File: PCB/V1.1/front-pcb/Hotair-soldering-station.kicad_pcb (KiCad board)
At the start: 2 copper layers, 70 x 120 mm, 60 parts, among them J2 main-board-conn, J3 hot_on, J4 solder_on, Q1 BC817, Q10 BC807, Q11 BC807, Q12 BC807, Q13 BC807, Q14 BC807, Q2 BC817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

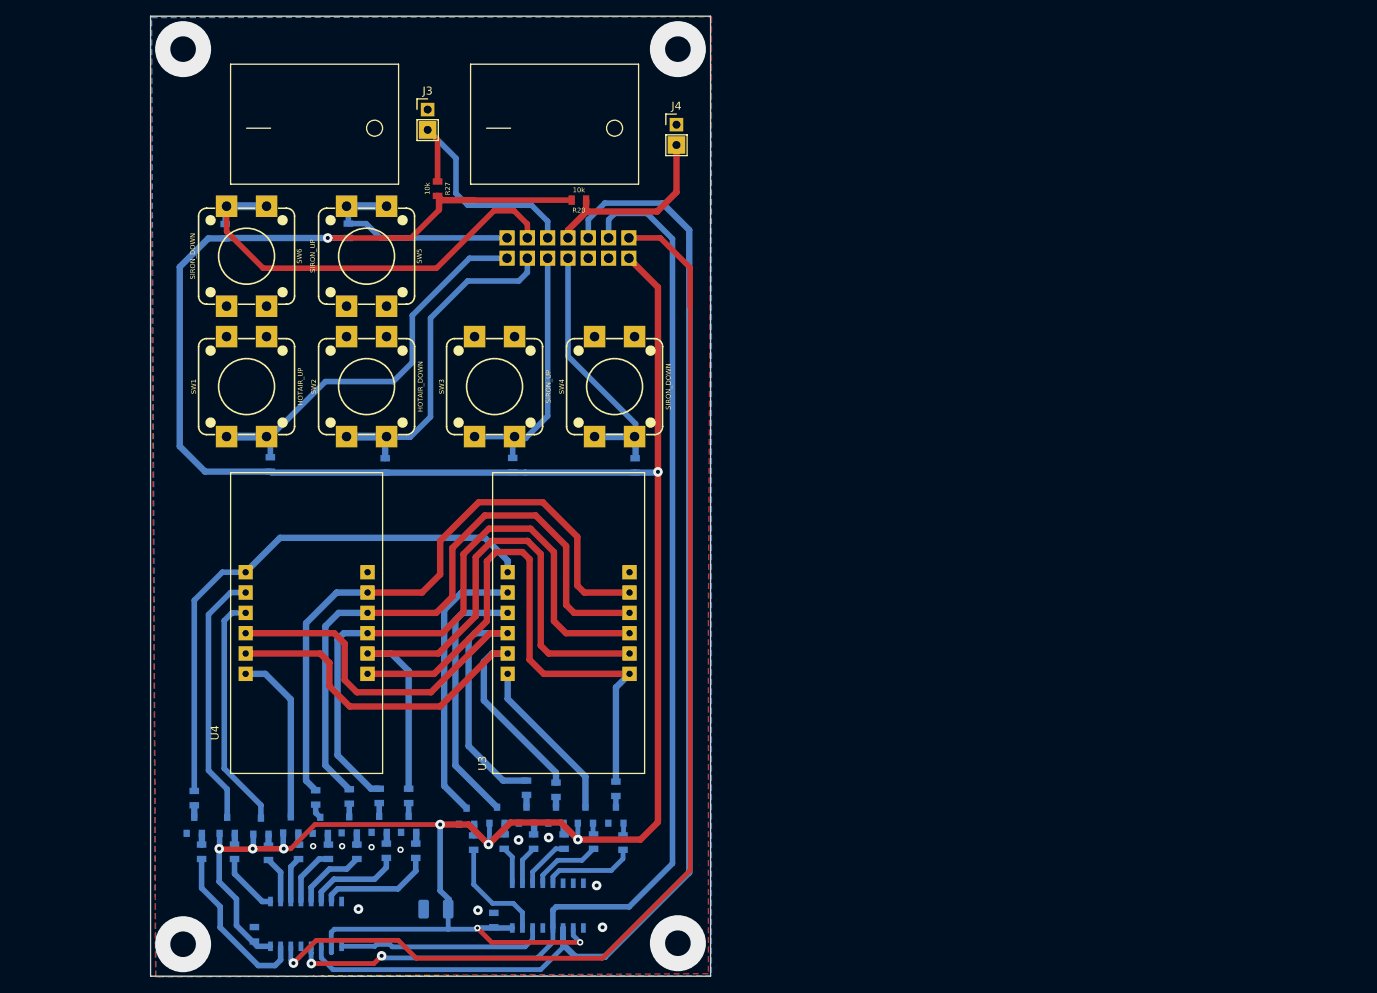
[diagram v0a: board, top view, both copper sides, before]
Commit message: Display change to LCD
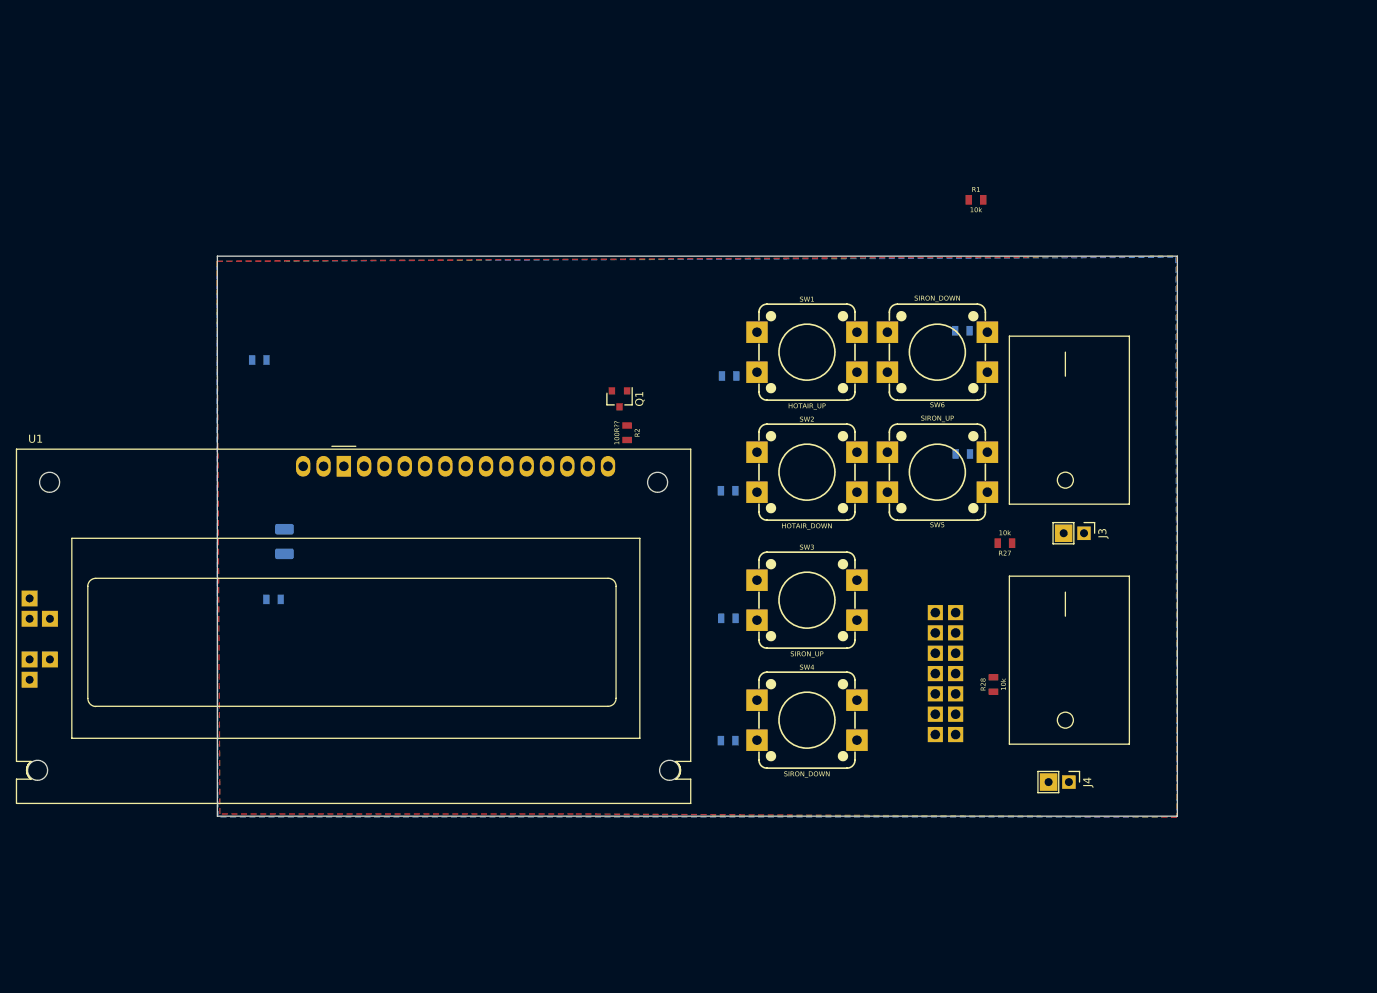
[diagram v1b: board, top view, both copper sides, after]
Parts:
- removed Q10, Q11, Q12, Q13, Q14, Q9: BC807, Package_TO_SOT_SMD:SOT-23
- removed Q2, Q3, Q4, Q5, Q6, Q7, Q8: BC817, Package_TO_SOT_SMD:SOT-23
- removed R10, R11, R12, R13, R14, R15, R16, R9: 120R, Capacitors:0805
- removed R17, R18, R19, R20, R21, R22, R3, R4, R5, R7, R8: 10k, Capacitors:0805
- removed R6: 5k6, Capacitors:0805
- removed U2: 74HC595D, Silicon-Standard:SO16
- removed U3: My-Footprints:3-digit-7-segment-display, My-Footprints:3-digit-7-segment-display
- removed U4: 3-dig-7-seg-display-common-anode, My-Footprints:3-digit-7-segment-display
- Q1, R1: moved to F.Cu
- R2: value 10k -> 100R??; moved to F.Cu
- U1: value 74HC595D -> RC1602A; footprint Silicon-Standard:SO16 -> Display:RC1602A; moved to F.Cu
- moved R1 109.8 mm to (126.4, 39.8), turned to 0 degrees
- moved J3 97.7 mm to (139.9, 81.4), turned to 270 degrees
- moved J4 95.7 mm to (138.1, 112.5), turned to 270 degrees
- moved R30 93.0 mm to (124.7, 56.1), turned to 180 degrees
- moved SW6 87.2 mm to (121.6, 58.8), turned to 180 degrees
- moved R27 83.6 mm to (130.1, 82.7), turned to 180 degrees
- moved R29 81.7 mm to (124.8, 71.5), turned to 180 degrees
- moved R28 79.7 mm to (128.6, 100.4), turned to 90 degrees
- moved SW5 76.3 mm to (121.6, 73.8), turned to 180 degrees
- moved C2 71.8 mm to (36.9, 59.8), turned to 0 degrees
- moved SW1 70.2 mm to (105.3, 58.8), turned to 0 degrees
- moved J2 68.8 mm to (119.5, 108.4), turned to 0 degrees
- moved R2 64.3 mm to (82.8, 68.9), turned to 270 degrees
- moved Q1 61.1 mm to (81.9, 64.6), turned to 270 degrees
- moved R23 58.4 mm to (95.6, 61.8), turned to 180 degrees
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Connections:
- J2 pad 12: 7SEG_CLK -> (no net)
- J2 pad 13: 7SEG_LATCH -> (no net)
- J2 pad 14: 7SEG_DIN -> (no net)
- J2 pad 2: GND -> +5V
- R1 pad 1: SEG_DP -> (no net)
- R2 pad 1: SEG_G -> Net-(Q1-Pad3)
- R2 pad 2: Net-(Q2-Pad1) -> Net-(R2-Pad2)
- U1 pad 1: HOTAIR_DIG3 -> GND
- U1 pad 10: +3V3 -> (no net)
- U1 pad 11: 7SEG_CLK -> (no net)
- U1 pad 12: 7SEG_LATCH -> (no net)
- U1 pad 13: GND -> (no net)
- U1 pad 14: 7SEG_DIN -> (no net)
- U1 pad 15: SEG_B -> +3V3
- U1 pad 16: +3V3 -> Net-(R2-Pad2)
- U1 pad 2: HOTAIR_DIG2 -> +5V
- U1 pad 3: HOTAIR_DIG1 -> (no net)
- U1 pad 4: SEG_G -> (no net)
- U1 pad 5: SEG_C -> (no net)
- U1 pad 6: SEG_DP -> (no net)
- U1 pad 7: SEG_D -> (no net)
- U1 pad 8: GND -> (no net)
- U1 pad 9: Net-(U1-Pad9) -> (no net)
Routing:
- net +3V3: track 357.2 -> 0.00 mm, vias 10 -> 0
- net 7SEG_CLK: track 156.2 -> 0.00 mm
- net 7SEG_LATCH: track 145.1 -> 0.00 mm, vias 2 -> 0
- net 7SEG_DIN: track 143.0 -> 0.00 mm, vias 1 -> 0
- net Net-(R10-Pad2): track 78.8 -> 0.00 mm
- net Net-(R9-Pad2): track 78.4 -> 0.00 mm
- net Net-(R14-Pad2): track 78.3 -> 0.00 mm
- net Net-(R13-Pad2): track 76.2 -> 0.00 mm
- net Net-(R12-Pad2): track 71.3 -> 0.00 mm
- net Net-(R11-Pad2): track 69.1 -> 0.00 mm
- net Net-(R15-Pad2): track 68.9 -> 0.00 mm
- net Net-(R16-Pad2): track 62.2 -> 0.00 mm
- net HOTAIR_FAN_DOWN_SW: track 56.1 -> 0.00 mm
- net HOTAIR_UP_SW: track 49.9 -> 0.00 mm
- net HOTAIR_DOWN_SW: track 42.8 -> 0.00 mm
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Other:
- board size 70 x 120 mm -> 120 x 70 mm

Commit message: Pin assign to new STM32F103, front panel design to new case
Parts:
- removed C1, C2: 100n, Capacitors:0805
- removed C3: 47u, Capacitor_Tantalum_SMD:CP_EIA-3528-21_Kemet-B
- removed Q1: BC817, Package_TO_SOT_SMD:SOT-23
- removed U1: RC1602A, Display:RC1602A
- added J1: solder_select, Connector_PinHeader_2.54mm:PinHeader_1x02_P2.54mm_Vertical, F.Cu at (92.7, 93.1)
- added R3: 10k, Capacitors:0805, F.Cu at (88.0, 79.8)
- added R4: 10k, Capacitors:0805, F.Cu at (83.9, 82.4)
- added SW7: SIRON_DOWN, Switches:TACTILE_SWITCH_PTH_12MM, F.Cu at (76.8, 103.5)
- added SW8: SIRON_UP, Switches:TACTILE_SWITCH_PTH_12MM, F.Cu at (42.5, 104.1)
- added SW9: SIRON_DOWN, Switches:TACTILE_SWITCH_PTH_12MM, F.Cu at (59.1, 104.1)
- R2: value 100R?? -> 10k
- moved R1 83.9 mm to (68.3, 100.2)
- moved R2 10.9 mm to (83.9, 79.8), turned to 0 degrees
- moved J2 4.81 mm to (119.5, 113.2)
- moved R28 4.81 mm to (128.6, 105.2)
- moved R24 4.81 mm to (95.5, 96.9)
- moved R26 4.81 mm to (95.5, 112.2)
- moved SW3 4.81 mm to (105.3, 94.6)
- moved SW4 4.81 mm to (105.3, 109.6)
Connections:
- J2 pad 10: HOTAIR_ON_SW -> HOTAIR_DOWN_SW
- J2 pad 11: SOLDER_ON_SW -> HOTAIR_UP_SW
- J2 pad 12: (no net) -> SOLDER_SELECT_SW
- J2 pad 13: (no net) -> HOTAIR_ON_SW
- J2 pad 14: (no net) -> SOLDER_ON_SW
- J2 pad 2: +5V -> GND
- J2 pad 3: GND -> MENU_DOWN_SW
- J2 pad 4: SOLDER_DOWN_SW -> MENU_OK_SW
- J2 pad 5: SOLDER_UP_SW -> MENU_UP_SW
- J2 pad 6: HOTAIR_DOWN_SW -> SOLDER_DOWN_SW
- J2 pad 7: HOTAIR_UP_SW -> SOLDER_UP_SW
- R1 pad 1: (no net) -> MENU_DOWN_SW
- R1 pad 2: Net-(Q1-Pad1) -> +3V3
- R2 pad 1: Net-(Q1-Pad3) -> MENU_OK_SW
- R2 pad 2: Net-(R2-Pad2) -> +3V3
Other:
- net class Default removed

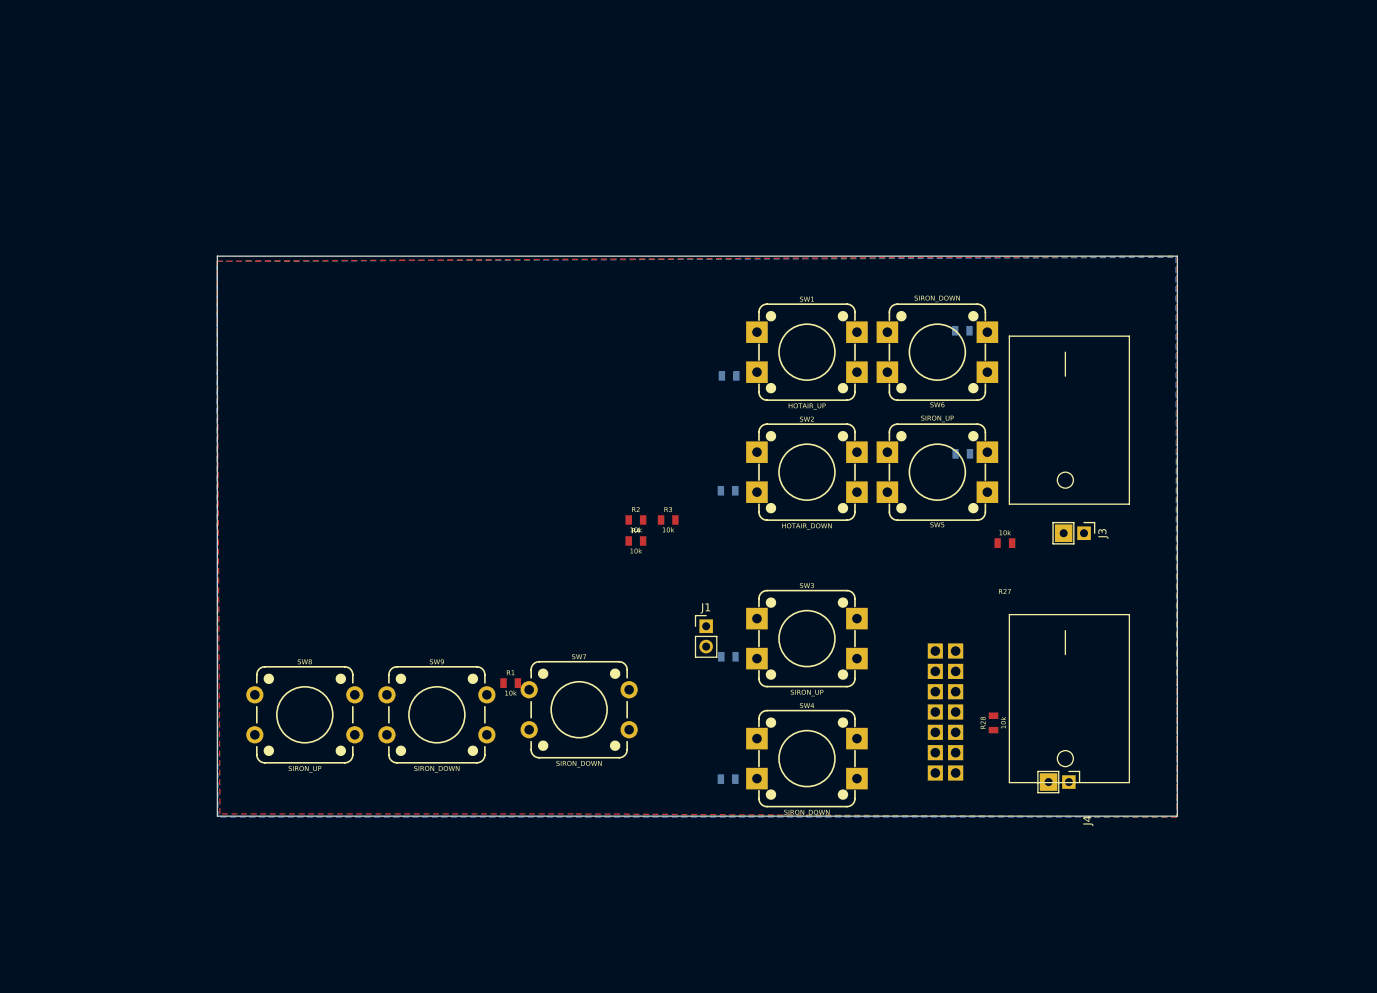
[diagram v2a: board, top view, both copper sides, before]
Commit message: Front Panel PCB design
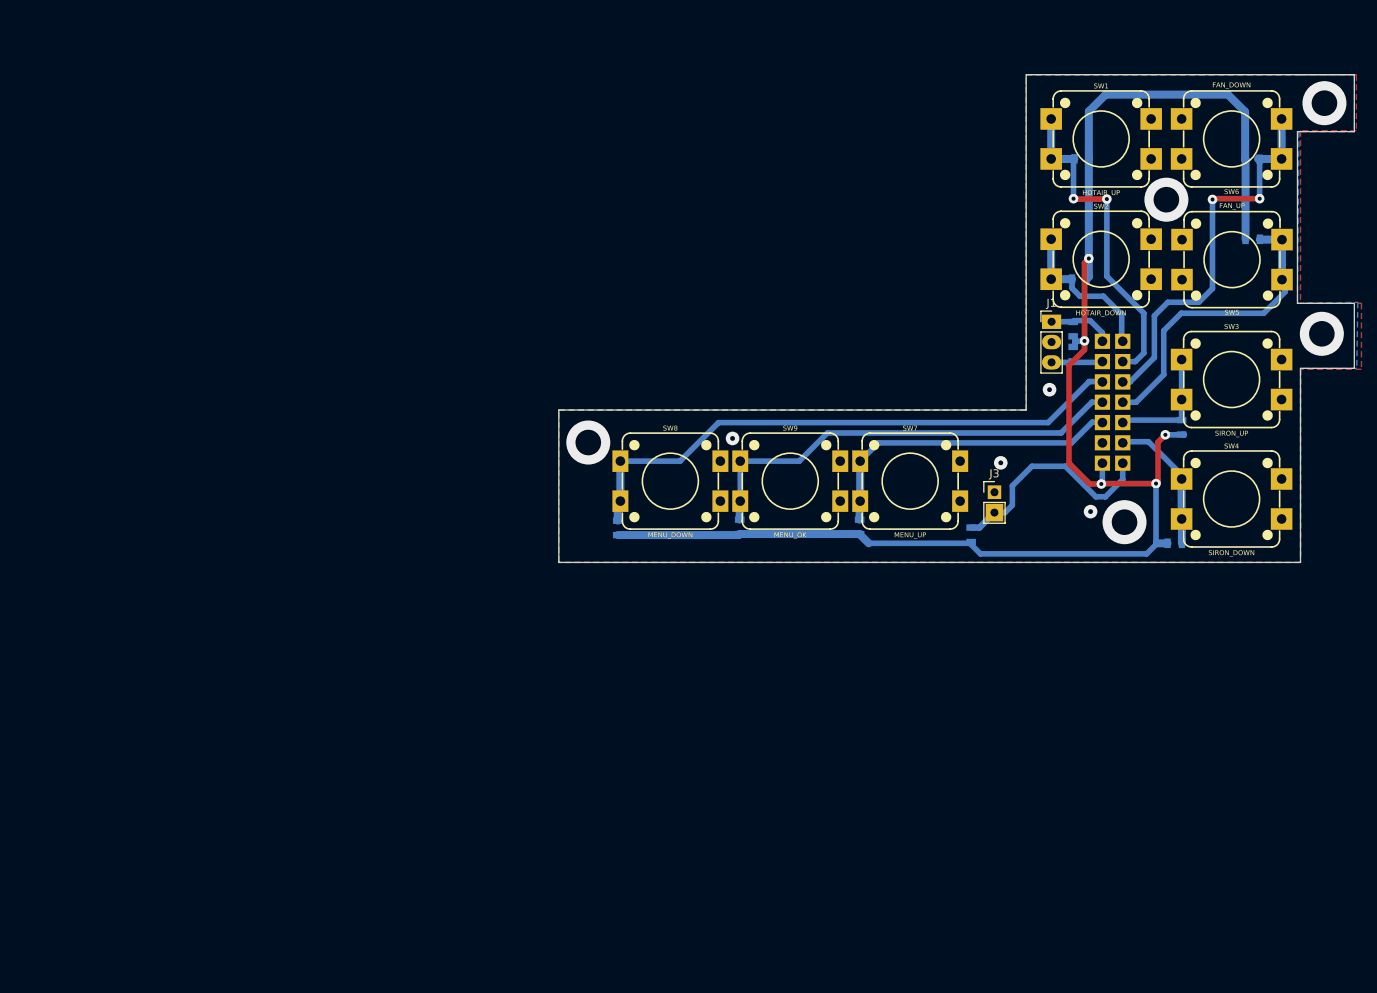
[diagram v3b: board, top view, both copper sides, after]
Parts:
- removed J4: solder_on, Connector_PinHeader_2.54mm:PinHeader_1x02_P2.54mm_Vertical
- J1: value solder_select -> Conn_01x03; footprint Connector_PinHeader_2.54mm:PinHeader_1x02_P2.54mm_Vertical -> Connector_PinHeader_2.54mm:PinHeader_1x03_P2.54mm_Vertical
- R1, R2, R27, R28, R3, R4: moved to B.Cu
- SW5: value SIRON_UP -> FAN_UP
- SW6: value SIRON_DOWN -> FAN_DOWN
- SW7: value SIRON_DOWN -> MENU_UP; footprint Switches:TACTILE_SWITCH_PTH_12MM -> My-Footprints:TACTILE_SWITCH_PTH_12MM
- SW8: value SIRON_UP -> MENU_DOWN; footprint Switches:TACTILE_SWITCH_PTH_12MM -> My-Footprints:TACTILE_SWITCH_PTH_12MM
- SW9: value SIRON_DOWN -> MENU_OK; footprint Switches:TACTILE_SWITCH_PTH_12MM -> My-Footprints:TACTILE_SWITCH_PTH_12MM
- moved R24 63.5 mm to (152.1, 68.2), turned to -90 degrees
- moved R26 63.1 mm to (151.3, 82.7)
- moved SW4 62.2 mm to (158.4, 77.2)
- moved SW3 62.2 mm to (158.4, 62.2)
- moved R4 60.7 mm to (138.6, 55.9), turned to -90 degrees
- moved J1 57.6 mm to (135.9, 55.0)
- moved SW8 54.2 mm to (88.2, 74.9)
- moved SW9 53.0 mm to (103.2, 74.9)
- moved R23 51.8 mm to (139.6, 34.6), turned to 0 degrees
- moved R25 51.2 mm to (139.3, 49.7), turned to 0 degrees
- moved SW7 50.3 mm to (118.2, 74.9)
- moved R28 47.2 mm to (138.6, 59.1)
- moved SW6 45.4 mm to (158.4, 32.2)
- moved SW1 45.4 mm to (142.1, 32.2)
- moved SW5 45.4 mm to (158.4, 47.2)
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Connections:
- J1 pad 1: GND -> WEP_ON_SW
- J1 pad 2: SOLDER_SELECT_SW -> GND
- J2 pad 10: HOTAIR_DOWN_SW -> HOTAIR_FAN_DOWN_SW
- J2 pad 11: HOTAIR_UP_SW -> HOTAIR_FAN_UP_SW
- J2 pad 12: SOLDER_SELECT_SW -> SOLDER_UP_SW
- J2 pad 13: HOTAIR_ON_SW -> SOLDER_DOWN_SW
- J2 pad 14: SOLDER_ON_SW -> HOTAIR_ON_SW
- J2 pad 3: MENU_DOWN_SW -> MENU_UP_SW
- J2 pad 5: MENU_UP_SW -> MENU_DOWN_SW
- J2 pad 6: SOLDER_DOWN_SW -> T12_ON_SW
- J2 pad 7: SOLDER_UP_SW -> WEP_ON_SW
- J2 pad 8: HOTAIR_FAN_UP_SW -> HOTAIR_DOWN_SW
- J2 pad 9: HOTAIR_FAN_DOWN_SW -> HOTAIR_UP_SW
- R28 pad 1: SOLDER_ON_SW -> T12_ON_SW
- R4 pad 1: SOLDER_SELECT_SW -> WEP_ON_SW
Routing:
- net +3V3: track 0.00 -> 189.0 mm, vias 0 -> 5
- net MENU_DOWN_SW: track 0.00 -> 72.1 mm
- net MENU_OK_SW: track 0.00 -> 55.7 mm
- net HOTAIR_FAN_DOWN_SW: track 0.00 -> 49.1 mm, vias 0 -> 2
- net HOTAIR_UP_SW: track 0.00 -> 41.3 mm, vias 0 -> 2
- net MENU_UP_SW: track 0.00 -> 39.5 mm
- net HOTAIR_FAN_UP_SW: track 0.00 -> 38.4 mm
- net HOTAIR_ON_SW: track 0.00 -> 28.1 mm
- net HOTAIR_DOWN_SW: track 0.00 -> 19.9 mm
- net SOLDER_DOWN_SW: track 0.00 -> 17.4 mm
- net SOLDER_UP_SW: track 0.00 -> 15.0 mm
- net WEP_ON_SW: track 0.00 -> 7.84 mm
- net T12_ON_SW: track 0.00 -> 6.37 mm
- net GND: vias 0 -> 9
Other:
- board size 120 x 70 mm -> 99.4 x 61 mm
